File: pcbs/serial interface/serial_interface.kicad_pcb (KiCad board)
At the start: 2 copper layers, 65 x 51 mm, 38 parts, among them J1 AFBR-1624Z, J2 AFBR-2624Z, U1 MM232R, U2 UMFT234XF, U3 74LVC1G14, U33 LTC6993xS6-2, U4 74LVC1G14, U5 LTC6993xS6-2

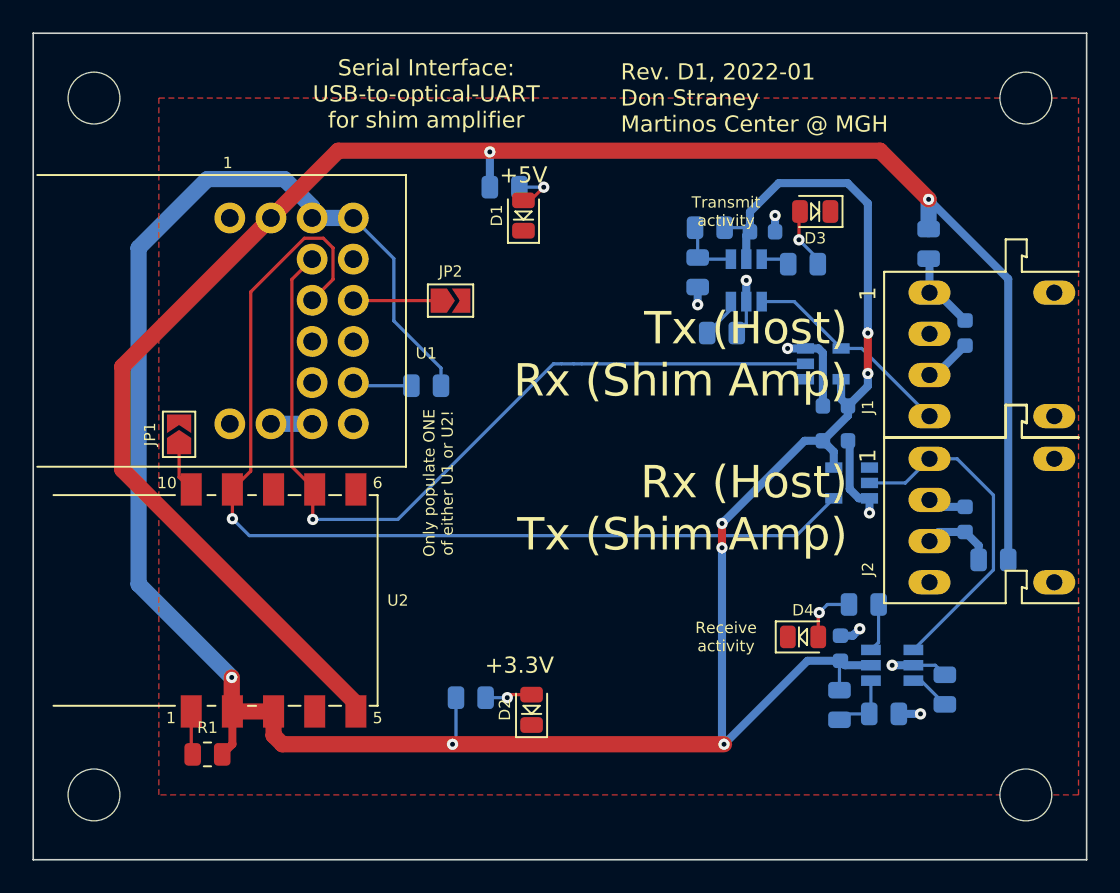
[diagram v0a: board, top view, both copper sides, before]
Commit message: Serial interface speed improvement
Upgraded serial interface to KiCAD 7.0
Replaced USB-serial modules with higher-speed (12 Mbps) one (#7)
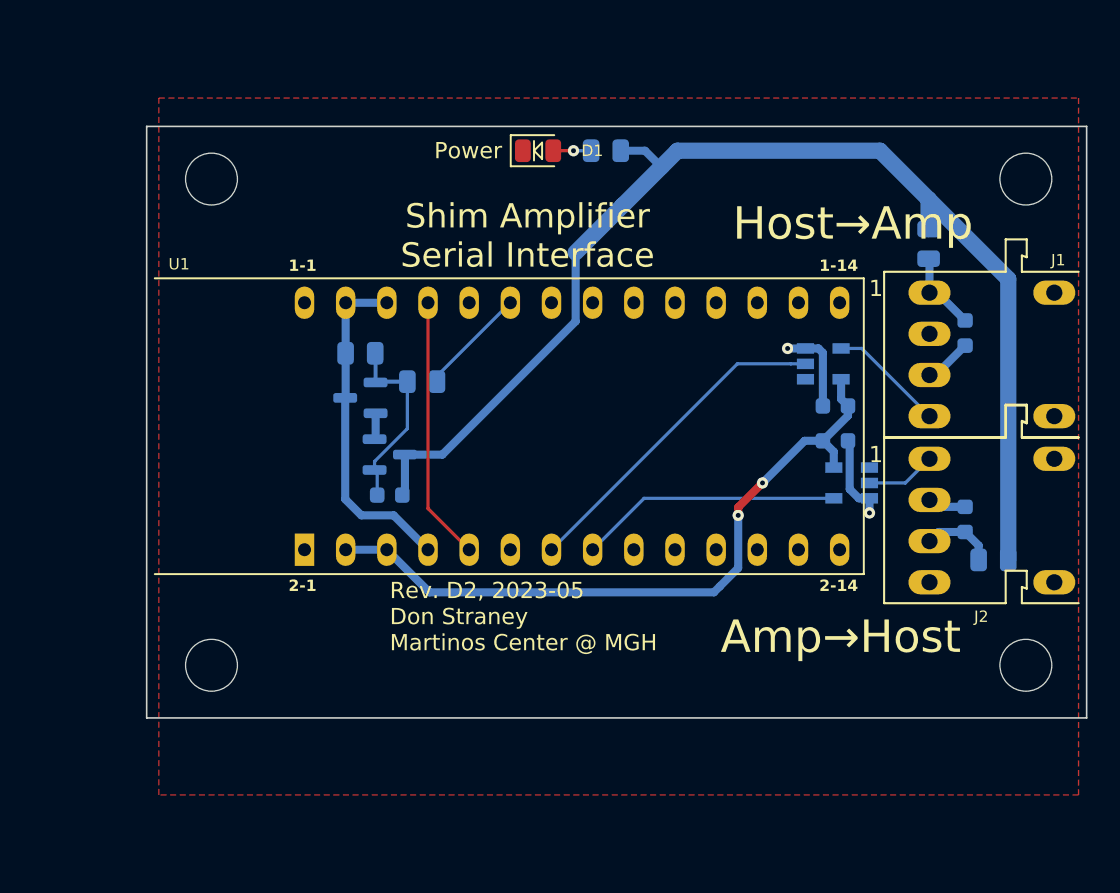
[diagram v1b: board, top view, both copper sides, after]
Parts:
- removed C6: 1uF 16V X7R, Capacitor_SMD:C_0603_1608Metric
- removed D2: Green, Martinos_std:LED_0805_2012Metric
- removed D3, D4: Yellow, Martinos_std:LED_0805_2012Metric
- removed JP1, JP2: SolderJumper_2_Open, Jumper:SolderJumper-2_P1.3mm_Open_TrianglePad1.0x1.5mm
- removed R10, R14, R6: 1K, Resistor_SMD:R_0805_2012Metric
- removed R11, R7: 10K, Resistor_SMD:R_0805_2012Metric
- removed R12, R8: 6.81K, Resistor_SMD:R_0805_2012Metric
- removed R13, R9: 180K, Resistor_SMD:R_0805_2012Metric
- removed U2: UMFT234XF, Martinos:FTDI_UMFT234XF
- removed U33, U5: LTC6993xS6-2, Martinos_std:TSOT-23-6
- added Q1: ??, Package_TO_SOT_SMD:SOT-23, B.Cu at (124.2, 106.5)
- added Q2: ??, Package_TO_SOT_SMD:SOT-23, B.Cu at (126.0, 110.0)
- C5: value 1uF 16V X7R -> 100nF 50V X7R
- R1: value DNP -> 100K; moved to B.Cu
- R2: value DNP -> 1K
- U1: value MM232R -> UM232H; footprint Martinos:FTDI_MM232R -> Don:FTDI_UM232H
- moved C5 28.2 mm to (126.0, 112.5), turned to 0 degrees
- moved R1 26.5 mm to (124.2, 103.8)
- moved U1 15.0 mm to (137.2, 108.2)
- moved H1 10.8 mm to (115.0, 123.0)
- moved H2 8.81 mm to (115.0, 93.0)
- moved H3 8.00 mm to (165.2, 123.0)
- moved R5 6.64 mm to (139.3, 91.2), turned to 180 degrees
- moved H4 5.00 mm to (165.2, 93.0)
- moved D1 4.10 mm to (135.2, 91.2), turned to 0 degrees
- moved R2 0.35 mm to (128.0, 105.5)
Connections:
- net /Rx activity indicator/In renamed Net-(J2-Data_Out)
- net /Tx activity indicator/In renamed Net-(J1-Data_in)
- C5 pad 1: GND -> Net-(Q1-G)
- C5 pad 2: +3V3 -> +5V
- R1 pad 1: Net-(R1-Pad1) -> Net-(Q1-D)
- R1 pad 2: +3V3 -> Net-(Q1-G)
- R2 pad 1: Net-(R2-Pad1) -> Net-(Q1-G)
- R2 pad 2: +3V3 -> /~{PWREN}
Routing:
- net +3V3: track 165.8 -> 43.2 mm, vias 7 -> 2
- net /Rx: track 63.4 -> 16.2 mm, vias 1 -> 0
- net +5V: track 112.1 -> 75.4 mm, vias 2 -> 0
- net /Tx: track 51.6 -> 20.4 mm, vias 1 -> 0
- net Net-(Q1-D): track 0.00 -> 21.1 mm
- net Net-(J2-Data_Out): track 20.8 -> 4.32 mm
- net Net-(U1-PU1): track 0.00 -> 16.3 mm
- net GND: track 28.0 -> 16.3 mm, vias 8 -> 2
- net Net-(Q1-G): track 0.00 -> 11.7 mm
- net /~{PWREN}: track 0.00 -> 6.75 mm
- net Net-(J1-Data_in): track 13.3 -> 7.19 mm
- net Net-(JP2-Pad1): track 5.28 -> 0.00 mm
- net Net-(R11-Pad2): track 4.08 -> 0.00 mm
- net Net-(U33-Pad4): track 4.00 -> 0.00 mm
- net Net-(D3-Pad2): track 3.76 -> 0.00 mm, vias 1 -> 0
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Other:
- board size 65 x 51 mm -> 58 x 36.5 mm
- board text added: "Amp→Host"
- board text added: "Host→Amp"
- board text added: "Power"
- board text added: "Rev. D2, 2023-05 Don Straney Martinos Center @ MGH"
- board text added: "Shim Amplifier Serial Interface"
- board text removed: "+3.3V"
- board text removed: "+5V"
- board text removed: "Only populate ONE of either U1 or U2!"
- board text removed: "Receive activity"
- board text removed: "Rev. D1, 2022-01 Don Straney Martinos Center @ MGH"
- board text removed: "Rx (Host) Tx (Shim Amp)"
- board text removed: "Serial Interface: USB-to-optical-UART for shim amplifier"
- board text removed: "Transmit activity"
- board text removed: "Tx (Host) Rx (Shim Amp)"

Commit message: Moved all project-specific symbols & footprints into new "shim" libraries Updated projects to reference the new "shim" library
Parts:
- D1: footprint Martinos_std:LED_0805_2012Metric -> shim:LED_0805_2012Metric
- J1, J2: footprint Martinos:AFBR-xx2xZ -> shim:AFBR-xx2xZ
- U1: footprint Don:FTDI_UM232H -> shim:FTDI_UM232H
- U3, U4: footprint Martinos_std:SOT-23-5 -> Package_TO_SOT_SMD:SOT-23-5
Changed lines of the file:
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@@
 		(embedded_fonts no)
 	)
-	(footprint "Martinos:AFBR-xx2xZ"
+	(footprint "shim:AFBR-xx2xZ"
 		(layer "F.Cu")
 		(at 165.00388 103.82 -90)
@@
 		)
 		(embedded_fonts no)
-		(model ":Martinos:AFBR-1624Z.STEP"
+		(model ":shim:AFBR-1624Z.STEP"
 			(offset
 				(xyz 0 -5.6 0)
@@
 		)
 	)
-	(footprint "Don:FTDI_UM232H"
+	(footprint "shim:FTDI_UM232H"
 		(layer "F.Cu")
 		(at 137.25 108.25)
@@
 		(embedded_fonts no)
 	)
-	(footprint "Martinos:AFBR-xx2xZ"
+	(footprint "shim:AFBR-xx2xZ"
 		(layer "F.Cu")
 		(at 165.00388 114.07 -90)
@@
 		)
 		(embedded_fonts no)
-		(model ":Martinos:AFBR-1624Z.STEP"
+		(model ":shim:AFBR-1624Z.STEP"
 			(offset
 				(xyz 0 -5.6 0)
@@
 		)
 	)
-	(footprint "Martinos_std:LED_0805_2012Metric"
+	(footprint "shim:LED_0805_2012Metric"
 		(layer "F.Cu")
 		(at 135.15 91.25)
@@
 		)
 	)
-	(footprint "Martinos_std:SOT-23-5"
+	(footprint "Package_TO_SOT_SMD:SOT-23-5"
 		(layer "B.Cu")
 		(at 152.75 104.4)
@@
 		)
 	)
-	(footprint "Martinos_std:SOT-23-5"
+	(footprint "Package_TO_SOT_SMD:SOT-23-5"
 		(layer "B.Cu")
 		(at 154.5 111.75 180)

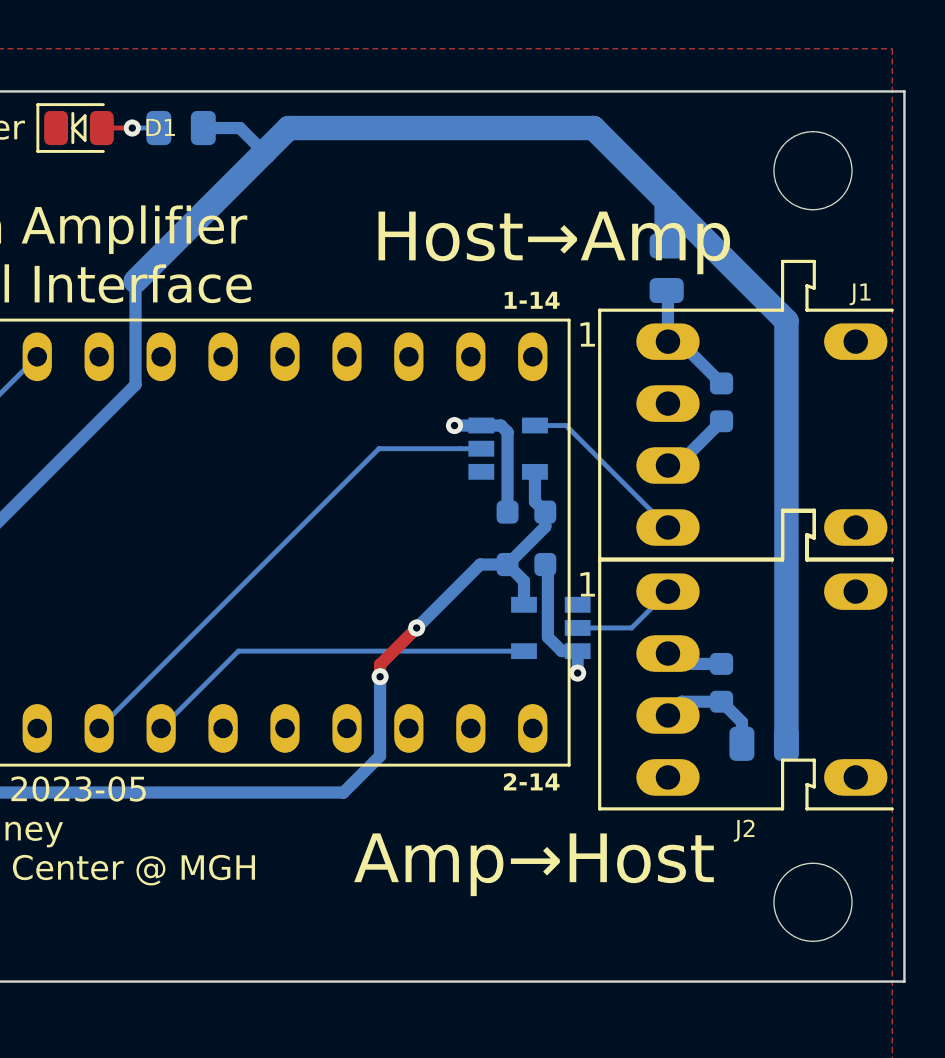
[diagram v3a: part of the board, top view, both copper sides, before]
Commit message: Tweaked serial interface and fiber control boards. Added empty manufacturing folder to indicate where to dump gerbers
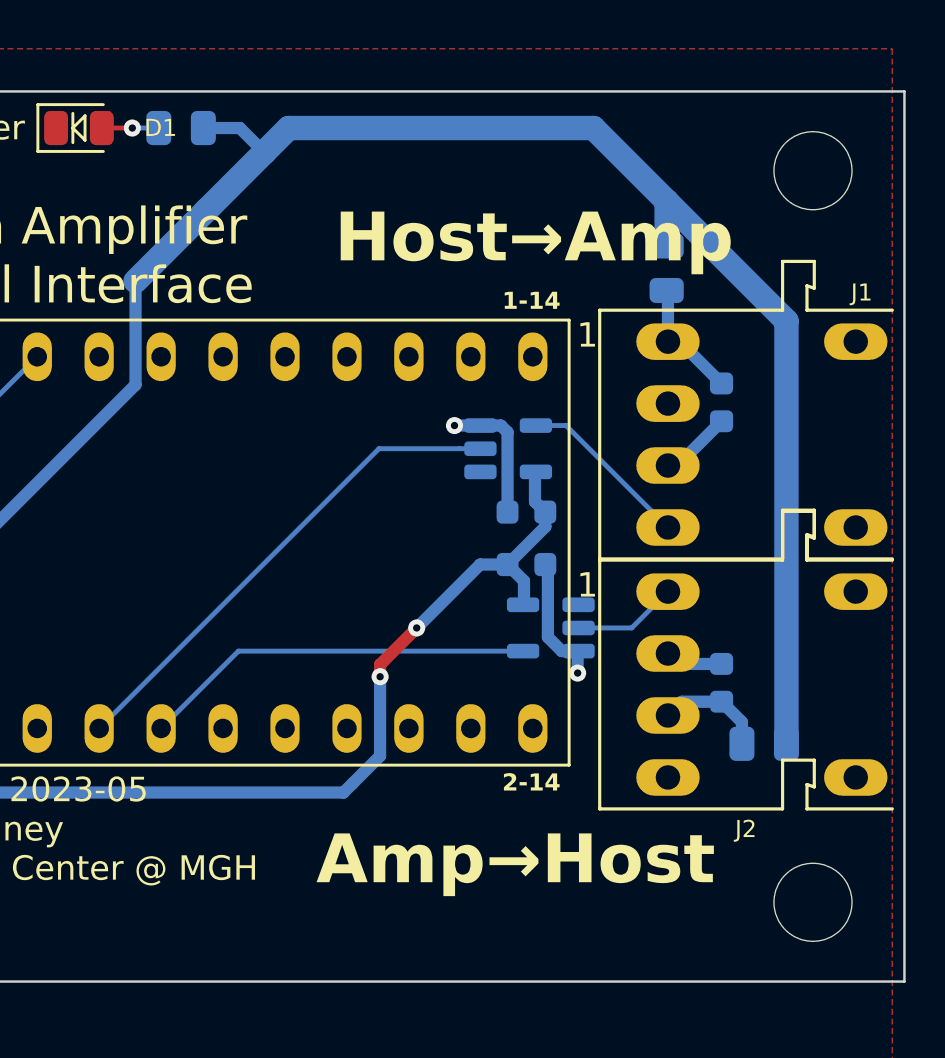
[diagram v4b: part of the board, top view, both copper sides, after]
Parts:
- Q1, Q2: value ?? -> DMG2305UX or similar
